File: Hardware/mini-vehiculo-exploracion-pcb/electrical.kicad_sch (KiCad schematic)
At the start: 16 parts, among them IC3 MAX8891EXK33_V+T, Q1 SI1467DH-T1-BE3, U4 TPS561208DDCR

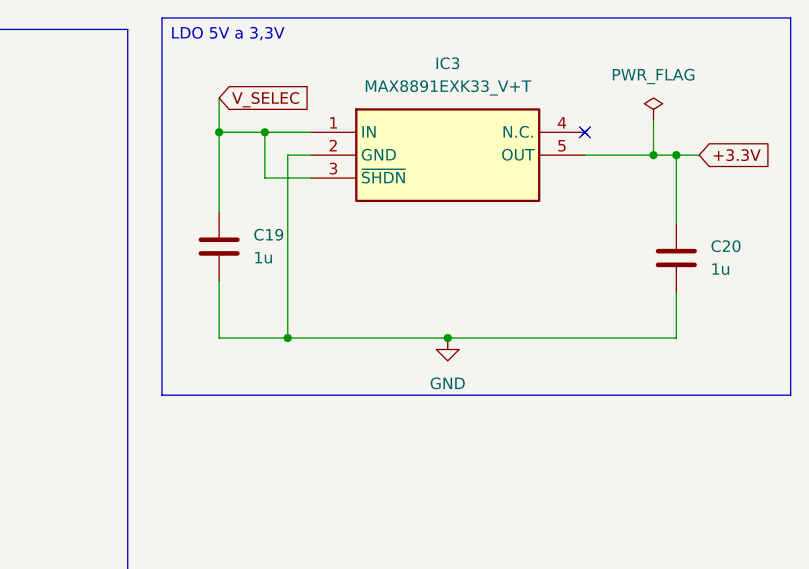
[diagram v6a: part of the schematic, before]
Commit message: Add footprints
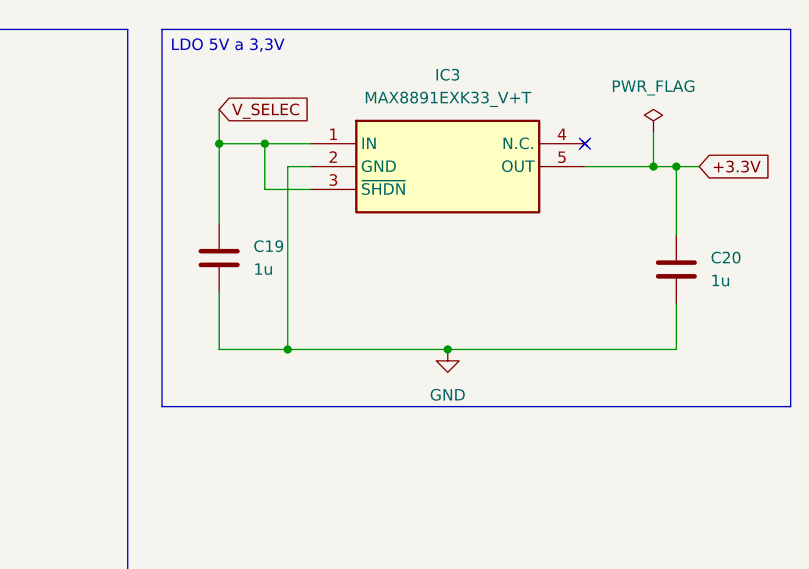
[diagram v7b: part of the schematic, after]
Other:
- moved on the sheet: C19, C20, IC3

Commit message: innit pcb
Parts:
- removed L1: 4,7u, symbol Device:L
- added L2: MLP2520S4R7MT0S1, MLP2520S4R7MT0S1:INDC2520X100N, symbol MLP2520S4R7MT0S1:MLP2520S4R7MT0S1
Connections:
- net V_BAT: now also L2.2
- net at C14.2, U4.2 (SW): now also L2.1
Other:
- moved on the sheet: C15, R13, R14
